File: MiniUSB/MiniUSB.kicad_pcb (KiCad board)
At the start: 2 copper layers, 21.8 x 14.5 mm, 7 parts, among them J1 USB_B_Micro, J2 Conn_01x05

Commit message: Part Numbers Added
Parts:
- J1: footprint Connector_USB:USB_Mini-B_Lumberg_2486_01_Horizontal -> SirBoardLibrary:SirBoard_USB_Mini-B
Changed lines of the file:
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@@
     (add_net "Net-(J1-Pad5)")
+  )
+  (module SirBoardLibrary:SirBoard_USB_Mini-B (layer F.Cu)
+    (at 65.532 31.877 180)
+    (descr "USB Mini-B 5-pin SMD connector, http://downloads.lumberg.com/datenblaetter/en/2486_01.pdf")
+    (tags "USB USB_B USB_Mini connector")
+    (attr smd)
+    (fp_text reference J1 (at 0 -5) (layer F.SilkS) hide
+      (effects (font (size 1 1) (thickness 0.15)))
+    )
+    (fp_text value USB_B_Micro (at 0 7.5) (layer F.Fab)
+      (effects (font (size 1 1) (thickness 0.15)))
+    )
+    (fp_line (start 2.35 -4.2) (end -2.35 -4.2) (layer F.CrtYd) (width 0.05))
+    (fp_line (start 2.35 -3.95) (end 2.35 -4.2) (layer F.CrtYd) (width 0.05))
+    (fp_line (start 4.35 1.5) (end 5.95 1.5) (layer F.CrtYd) (width 0.05))
+    (fp_line (start 4.35 4.2) (end 5.95 4.2) (layer F.CrtYd) (width 0.05))
+    (fp_line (start 4.35 6.35) (end 4.35 4.2) (layer F.CrtYd) (width 0.05))
+    (fp_line (start 3.91 5.91) (end -3.91 5.91) (layer F.SilkS) (width 0.12))
+    (fp_line (start -1.6 -2.85) (end -1.25 -3.35) (layer F.Fab) (width 0.1))
+    (fp_line (start -2.11 -3.41) (end -2.11 -3.84) (layer F.SilkS) (width 0.12))
+    (fp_text user %R (at 0 1.6 180) (layer F.Fab)
+      (effects (font (size 1 1) (thickness 0.15)))
+    )
+    (fp_line (start 3.91 5.91) (end 3.91 3.96) (layer F.SilkS) (width 0.12))
+    (fp_line (start 3.91 1.74) (end 3.91 -1.49) (layer F.SilkS) (width 0.12))
+    (fp_line (start 2.11 -3.41) (end 3.19 -3.41) (layer F.SilkS) (width 0.12))
+    (fp_line (start -3.19 -3.41) (end -2.11 -3.41) (layer F.SilkS) (width 0.12))
+    (fp_line (start -3.91 1.74) (end -3.91 -1.49) (layer F.SilkS) (width 0.12))
+    (fp_line (start -3.91 5.91) (end -3.91 3.96) (layer F.SilkS) (width 0.12))
+    (fp_line (start 3.85 5.85) (end 3.85 -3.35) (layer F.Fab) (width 0.1))
+    (fp_line (start -3.85 5.85) (end 3.85 5.85) (layer F.Fab) (width 0.1))
+    (fp_line (start -3.85 -3.35) (end -3.85 5.85) (layer F.Fab) (width 0.1))
+    (fp_line (start -3.85 -3.35) (end 3.85 -3.35) (layer F.Fab) (width 0.1))
+    (fp_line (start -4.35 6.35) (end 4.35 6.35) (layer F.CrtYd) (width 0.05))
+    (fp_line (start 5.95 -3.95) (end 2.35 -3.95) (layer F.CrtYd) (width 0.05))
+    (fp_line (start 5.95 1.5) (end 5.95 4.2) (layer F.CrtYd) (width 0.05))
+    (fp_line (start -1.95 -3.35) (end -1.6 -2.85) (layer F.Fab) (width 0.1))
+    (fp_line (start 4.35 -1.25) (end 4.35 1.5) (layer F.CrtYd) (width 0.05))
+    (fp_line (start 4.35 -1.25) (end 5.95 -1.25) (layer F.CrtYd) (width 0.05))
+    (fp_line (start 5.95 -3.95) (end 5.95 -1.25) (layer F.CrtYd) (width 0.05))
+    (fp_line (start -2.35 -3.95) (end -2.35 -4.2) (layer F.CrtYd) (width 0.05))
+    (fp_line (start -5.95 -3.95) (end -2.35 -3.95) (layer F.CrtYd) (width 0.05))
+    (fp_line (start -5.95 -3.95) (end -5.95 -1.25) (layer F.CrtYd) (width 0.05))
+    (fp_line (start -4.35 -1.25) (end -5.95 -1.25) (layer F.CrtYd) (width 0.05))
+    (fp_line (start -4.35 -1.25) (end -4.35 1.5) (layer F.CrtYd) (width 0.05))
+    (fp_line (start -4.35 1.5) (end -5.95 1.5) (layer F.CrtYd) (width 0.05))
+    (fp_line (start -5.95 1.5) (end -5.95 4.2) (layer F.CrtYd) (width 0.05))
+    (fp_line (start -4.35 4.2) (end -5.95 4.2) (layer F.CrtYd) (width 0.05))
+    (fp_line (start -4.35 6.35) (end -4.35 4.2) (layer F.CrtYd) (width 0.05))
+    (pad 5 smd rect (at 1.6 -2.65) (size 0.5 2.3) (layers F.Cu F.Paste F.Mask)
+      (net 1 "Net-(J1-Pad5)"))
+    (pad 4 smd rect (at 0.8 -2.65) (size 0.5 2.3) (layers F.Cu F.Paste F.Mask)
+      (net 2 "Net-(J1-Pad4)"))
+    (pad 1 smd rect (at -1.6 -2.65) (size 0.5 2.3) (layers F.Cu F.Paste F.Mask)
+      (net 5 "Net-(J1-Pad1)"))
+    (pad 2 smd rect (at -0.8 -2.65) (size 0.5 2.3) (layers F.Cu F.Paste F.Mask)
+      (net 4 "Net-(J1-Pad2)"))
+    (pad 3 smd rect (at 0 -2.65) (size 0.5 2.3) (layers F.Cu F.Paste F.Mask)
+      (net 3 "Net-(J1-Pad3)"))
+    (pad "" np_thru_hole circle (at -2.25 0) (size 1 1) (drill 1) (layers *.Cu *.Mask))
+    (pad "" np_thru_hole circle (at 2.15 0) (size 1 1) (drill 1) (layers *.Cu *.Mask))
+    (pad 6 smd rect (at -4.45 2.95) (size 2 2.5) (layers F.Cu F.Paste F.Mask)
+      (net 1 "Net-(J1-Pad5)"))
+    (pad 6 smd rect (at -4.45 -2.55) (size 2 2.5) (layers F.Cu F.Paste F.Mask)
+      (net 1 "Net-(J1-Pad5)"))
+    (pad 6 smd rect (at 4.45 -2.55) (size 2 2.5) (layers F.Cu F.Paste F.Mask)
+      (net 1 "Net-(J1-Pad5)"))
+    (pad 6 smd rect (at 4.45 2.95) (size 2 2.5) (layers F.Cu F.Paste F.Mask)
+      (net 1 "Net-(J1-Pad5)"))
+    (model ${KISYS3DMOD}/Connector_USB.3dshapes/USB_Mini-B_Lumberg_2486_01_Horizontal.wrl
+      (at (xyz 0 0 0))
+      (scale (xyz 1 1 1))
+      (rotate (xyz 0 0 0))
+    )
   )
   (module logo:logo63x89 (layer B.Cu)
@@
       (xy -0.0508 2.641214) (xy -0.0508 2.243667) (xy 0.059266 2.243667) (xy 0.059266 2.439106)) (layer F.SilkS) (width 0.01))
   )
-  (module Connector_USB:USB_Mini-B_Lumberg_2486_01_Horizontal (layer F.Cu)
-    (at 65.532 31.877 180)
-    (descr "USB Mini-B 5-pin SMD connector, http://downloads.lumberg.com/datenblaetter/en/2486_01.pdf")
-    (tags "USB USB_B USB_Mini connector")
-    (attr smd)
-    (fp_text reference J1 (at 0 -5) (layer F.SilkS) hide
-      (effects (font (size 1 1) (thickness 0.15)))
-    )
-    (fp_text value USB_B_Micro (at 0 7.5) (layer F.Fab)
-      (effects (font (size 1 1) (thickness 0.15)))
-    )
-    (fp_line (start -4.35 6.35) (end -4.35 4.2) (layer F.CrtYd) (width 0.05))
-    (fp_line (start -4.35 4.2) (end -5.95 4.2) (layer F.CrtYd) (width 0.05))
-    (fp_line (start -5.95 1.5) (end -5.95 4.2) (layer F.CrtYd) (width 0.05))
-    (fp_line (start -4.35 1.5) (end -5.95 1.5) (layer F.CrtYd) (width 0.05))
-    (fp_line (start -4.35 -1.25) (end -4.35 1.5) (layer F.CrtYd) (width 0.05))
-    (fp_line (start -4.35 -1.25) (end -5.95 -1.25) (layer F.CrtYd) (width 0.05))
-    (fp_line (start -5.95 -3.95) (end -5.95 -1.25) (layer F.CrtYd) (width 0.05))
-    (fp_line (start -5.95 -3.95) (end -2.35 -3.95) (layer F.CrtYd) (width 0.05))
-    (fp_line (start -2.35 -3.95) (end -2.35 -4.2) (layer F.CrtYd) (width 0.05))
-    (fp_line (start 5.95 -3.95) (end 5.95 -1.25) (layer F.CrtYd) (width 0.05))
-    (fp_line (start 4.35 -1.25) (end 5.95 -1.25) (layer F.CrtYd) (width 0.05))
-    (fp_line (start 4.35 -1.25) (end 4.35 1.5) (layer F.CrtYd) (width 0.05))
-    (fp_line (start -1.95 -3.35) (end -1.6 -2.85) (layer F.Fab) (width 0.1))
-    (fp_line (start 5.95 1.5) (end 5.95 4.2) (layer F.CrtYd) (width 0.05))
-    (fp_line (start 5.95 -3.95) (end 2.35 -3.95) (layer F.CrtYd) (width 0.05))
-    (fp_line (start -4.35 6.35) (end 4.35 6.35) (layer F.CrtYd) (width 0.05))
-    (fp_line (start -3.85 -3.35) (end 3.85 -3.35) (layer F.Fab) (width 0.1))
-    (fp_line (start -3.85 -3.35) (end -3.85 5.85) (layer F.Fab) (width 0.1))
-    (fp_line (start -3.85 5.85) (end 3.85 5.85) (layer F.Fab) (width 0.1))
-    (fp_line (start 3.85 5.85) (end 3.85 -3.35) (layer F.Fab) (width 0.1))
-    (fp_line (start -3.91 5.91) (end -3.91 3.96) (layer F.SilkS) (width 0.12))
-    (fp_line (start -3.91 1.74) (end -3.91 -1.49) (layer F.SilkS) (width 0.12))
-    (fp_line (start -3.19 -3.41) (end -2.11 -3.41) (layer F.SilkS) (width 0.12))
-    (fp_line (start 2.11 -3.41) (end 3.19 -3.41) (layer F.SilkS) (width 0.12))
-    (fp_line (start 3.91 1.74) (end 3.91 -1.49) (layer F.SilkS) (width 0.12))
-    (fp_line (start 3.91 5.91) (end 3.91 3.96) (layer F.SilkS) (width 0.12))
-    (fp_text user %R (at 0 1.6 180) (layer F.Fab)
-      (effects (font (size 1 1) (thickness 0.15)))
-    )
-    (fp_line (start -2.11 -3.41) (end -2.11 -3.84) (layer F.SilkS) (width 0.12))
-    (fp_line (start -1.6 -2.85) (end -1.25 -3.35) (layer F.Fab) (width 0.1))
-    (fp_line (start 3.91 5.91) (end -3.91 5.91) (layer F.SilkS) (width 0.12))
-    (fp_line (start 4.35 6.35) (end 4.35 4.2) (layer F.CrtYd) (width 0.05))
-    (fp_line (start 4.35 4.2) (end 5.95 4.2) (layer F.CrtYd) (width 0.05))
-    (fp_line (start 4.35 1.5) (end 5.95 1.5) (layer F.CrtYd) (width 0.05))
-    (fp_line (start 2.35 -3.95) (end 2.35 -4.2) (layer F.CrtYd) (width 0.05))
-    (fp_line (start 2.35 -4.2) (end -2.35 -4.2) (layer F.CrtYd) (width 0.05))
-    (pad "" np_thru_hole circle (at 2.2 0 180) (size 1 1) (drill 1) (layers *.Cu *.Mask))
-    (pad "" np_thru_hole circle (at -2.2 0 180) (size 1 1) (drill 1) (layers *.Cu *.Mask))
-    (pad 6 smd rect (at 4.45 2.85 180) (size 2 1.7) (layers F.Cu F.Paste F.Mask)
-      (net 1 "Net-(J1-Pad5)"))
-    (pad 6 smd rect (at 4.45 -2.6 180) (size 2 1.7) (layers F.Cu F.Paste F.Mask)
-      (net 1 "Net-(J1-Pad5)"))
-    (pad 6 smd rect (at -4.45 2.85 180) (size 2 1.7) (layers F.Cu F.Paste F.Mask)
-      (net 1 "Net-(J1-Pad5)"))
-    (pad 6 smd rect (at -4.45 -2.6 180) (size 2 1.7) (layers F.Cu F.Paste F.Mask)
-      (net 1 "Net-(J1-Pad5)"))
-    (pad 5 smd rect (at 1.6 -2.7 180) (size 0.5 2) (layers F.Cu F.Paste F.Mask)
-      (net 1 "Net-(J1-Pad5)"))
-    (pad 4 smd rect (at 0.8 -2.7 180) (size 0.5 2) (layers F.Cu F.Paste F.Mask)
-      (net 2 "Net-(J1-Pad4)"))
-    (pad 3 smd rect (at 0 -2.7 180) (size 0.5 2) (layers F.Cu F.Paste F.Mask)
-      (net 3 "Net-(J1-Pad3)"))
-    (pad 2 smd rect (at -0.8 -2.7 180) (size 0.5 2) (layers F.Cu F.Paste F.Mask)
-      (net 4 "Net-(J1-Pad2)"))
-    (pad 1 smd rect (at -1.6 -2.7 180) (size 0.5 2) (layers F.Cu F.Paste F.Mask)
-      (net 5 "Net-(J1-Pad1)"))
-    (model ${KISYS3DMOD}/Connector_USB.3dshapes/USB_Mini-B_Lumberg_2486_01_Horizontal.wrl
-      (at (xyz 0 0 0))
-      (scale (xyz 1 1 1))
-      (rotate (xyz 0 0 0))
-    )
-  )
   (module MountingHole:MountingHole_2.7mm_M2.5_ISO14580_Pad (layer F.Cu)

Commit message: Board Redesign
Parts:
- removed the G*** at (57.4, 34.9)
- removed the H1 at (73.7, 28.3)
- added H1: MountingHole, SirBoardLibrary:MountingHole_M2.5_SirBoard, F.Cu at (74.9, 37.5)
- added H1: MountingHole, SirBoardLibrary:MountingHole_M2.5_SirBoard, F.Cu at (57.1, 37.5)
- added H1: MountingHole, SirBoardLibrary:MountingHole_M2.5_SirBoard, F.Cu at (57.1, 27.3)
- H2: footprint MountingHole:MountingHole_2.7mm_M2.5_ISO14580_Pad -> SirBoardLibrary:MountingHole_M2.5_SirBoard
- J1: value USB_B_Micro -> USB_B_Mini
- moved H2 17.6 mm to (74.9, 27.3), turned to 0 degrees
- moved G*** 1.14 mm to (66.0, 33.7)
- moved J1 1.14 mm to (66.0, 30.9)
- moved G*** 0.81 mm to (66.0, 28.4)
- moved J2 0.51 mm to (71.1, 38.5)
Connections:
- net Net-(J1-Pad1) renamed /VBus
- net Net-(J1-Pad2) renamed /D-
- net Net-(J1-Pad3) renamed /D+
- net Net-(J1-Pad4) renamed /ID
- net Net-(J1-Pad5) renamed /GND
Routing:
- net /VBus: track 5.95 -> 6.96 mm
- net /D+: track 3.90 -> 4.92 mm
- net /ID: track 4.62 -> 5.64 mm
- net /D-: track 4.62 -> 5.64 mm
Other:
- board size 21.8 x 14.5 mm -> 22.9 x 15.2 mm
- board text added: "www.SirBoard.com"

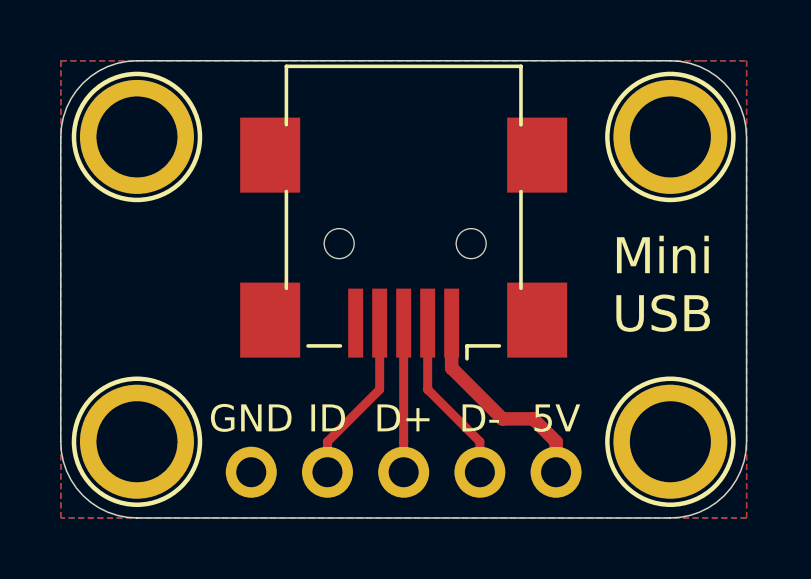
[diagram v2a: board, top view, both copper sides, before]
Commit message: Breakout Boards Revision 2
Renders updated, silkscreen text improved, blurry silkscreen items removed/resized.
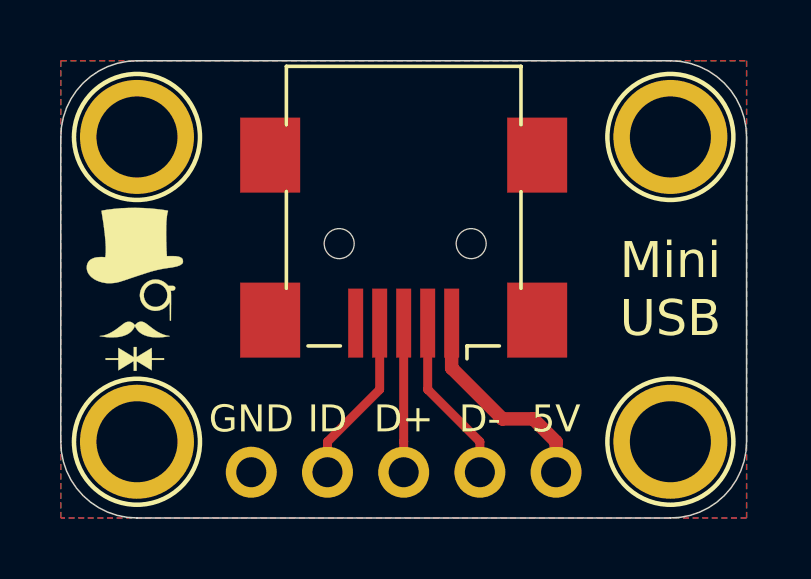
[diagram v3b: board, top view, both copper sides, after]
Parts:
- added G***: LOGO, logo:logo54x76, F.Cu at (57.1, 32.4)
